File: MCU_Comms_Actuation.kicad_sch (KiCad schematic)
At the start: 46 parts, among them J1 MTSW-105-09-L-S-480, J2 U.FL-R-SMT-1_80_, Y2 C3E-8.000-18-3030-X-R

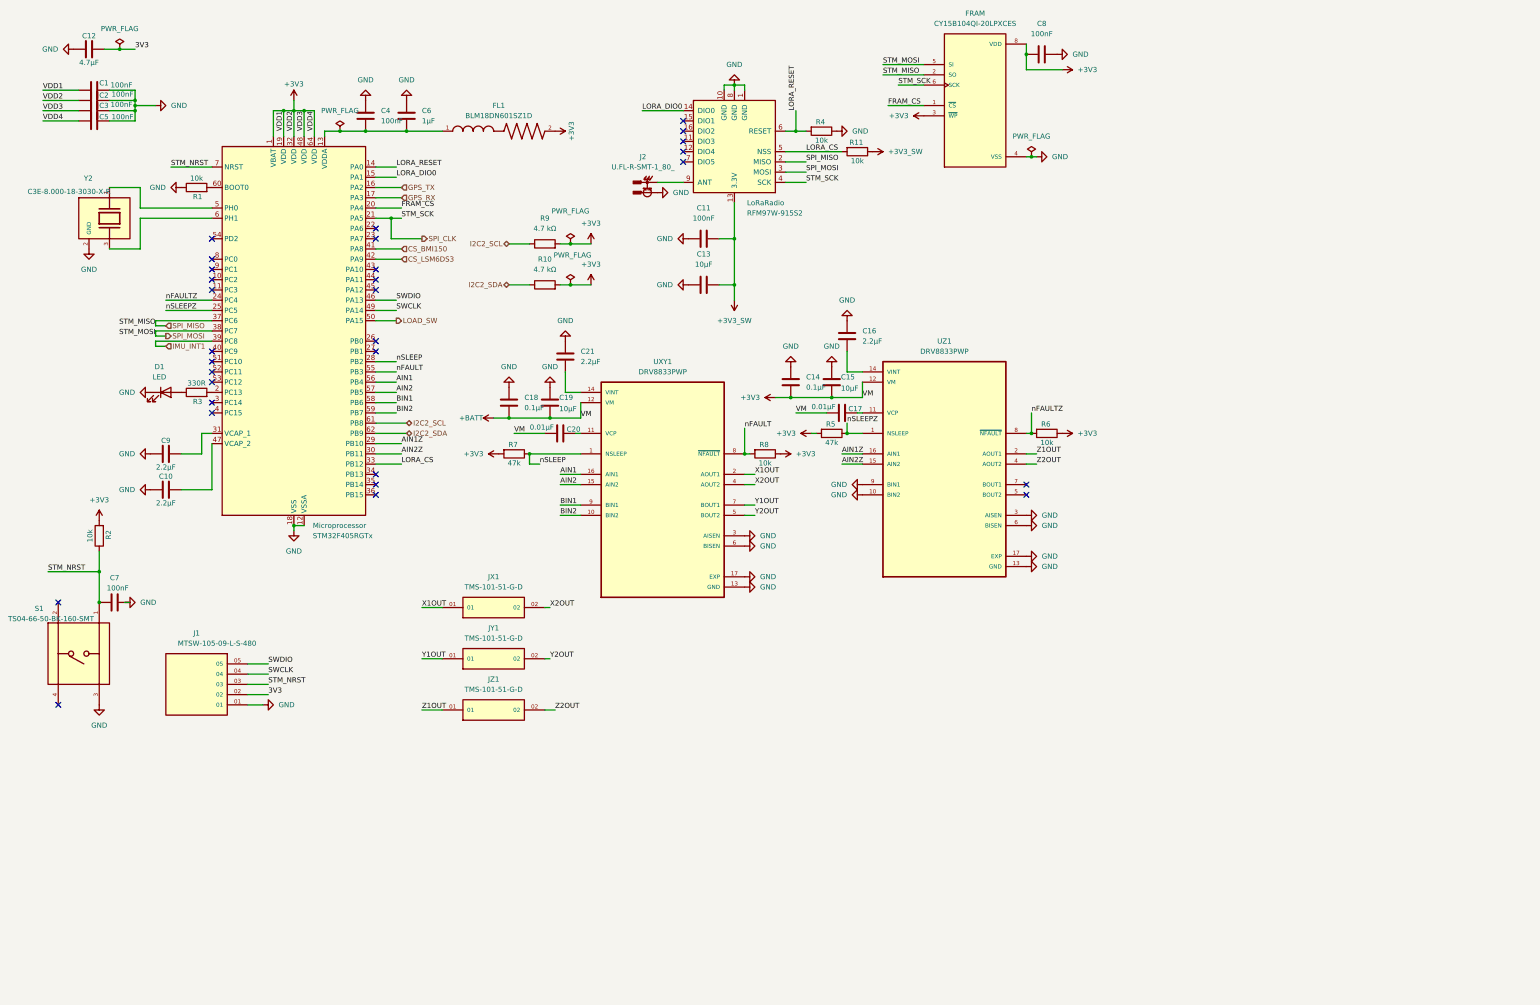
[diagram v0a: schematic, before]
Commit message: Add XYZ photodiodes to sun sensor. Fix hierarchical labels on MCU.
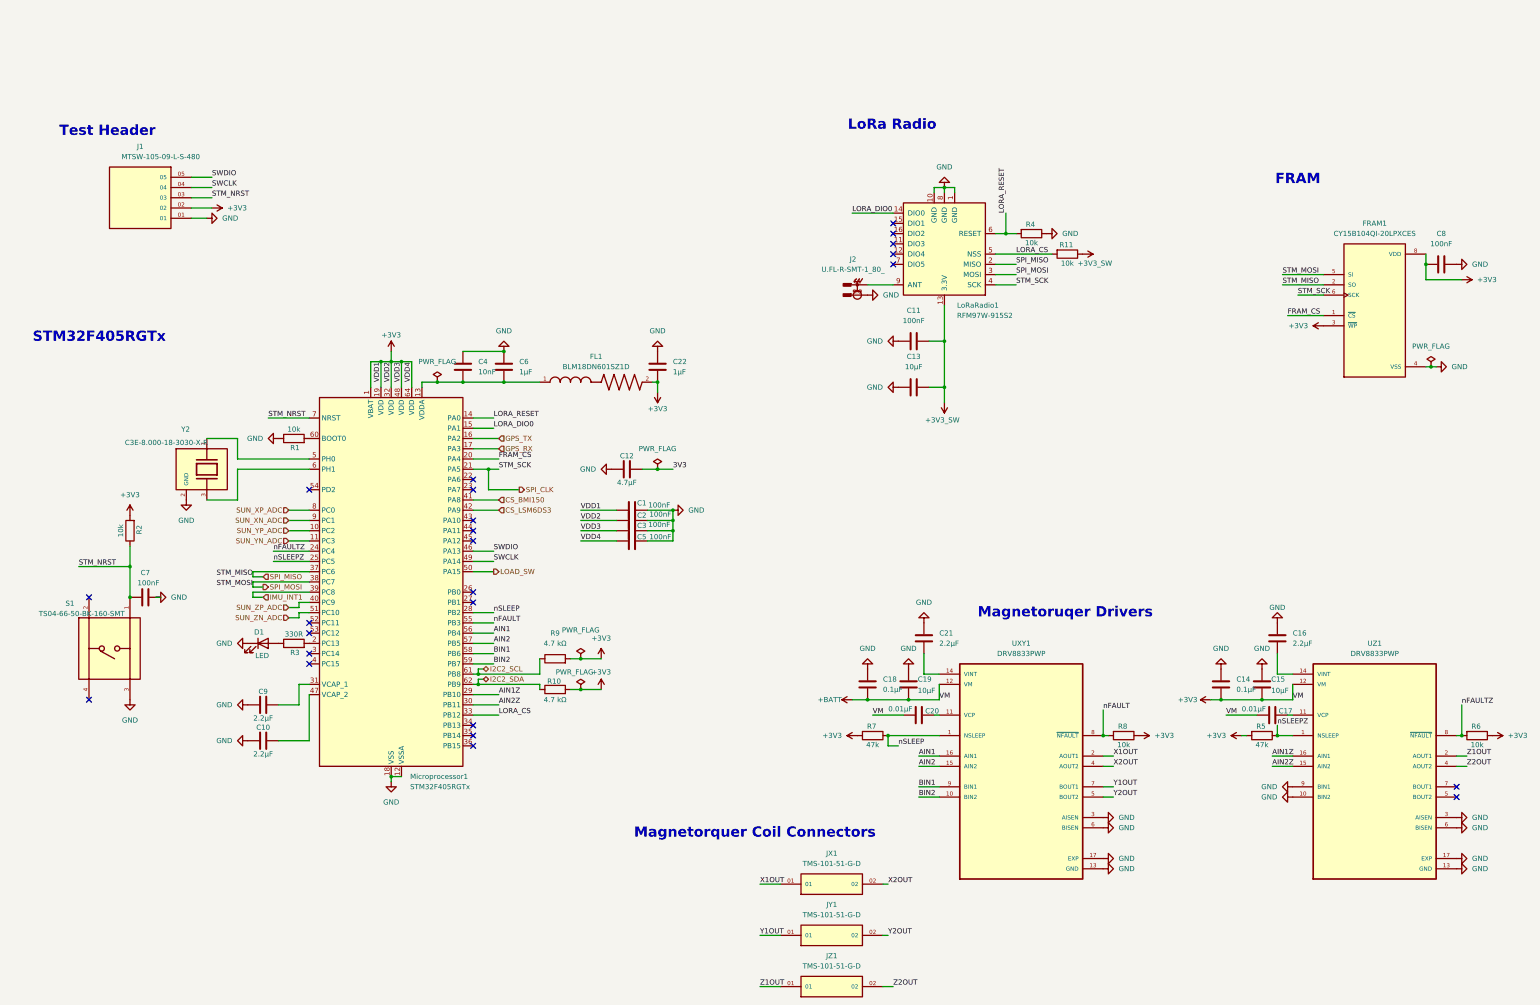
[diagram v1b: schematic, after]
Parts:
- added C22: 1µF, Capacitor_SMD:C_0603_1608Metric, symbol Device:C
- C4: value 100nF -> 10nF
- renumbered FRAM to FRAM1, LoRaRadio to LoRaRadio1, Microprocessor to Microprocessor1
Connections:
- net +3V3: now also J1.02, C22.2
- net 3V3: no longer J1.02
- net GND: now also C22.1
- net SUN_YP_ADC: now reaches Microprocessor1.10 (PC2)
- net SUN_YN_ADC: now reaches Microprocessor1.11 (PC3)
- net SUN_ZP_ADC: now reaches Microprocessor1.40 (PC9)
- net SUN_ZN_ADC: now reaches Microprocessor1.51 (PC10)
- net SUN_XP_ADC: now reaches Microprocessor1.8 (PC0)
- net SUN_XN_ADC: now reaches Microprocessor1.9 (PC1)
- no-connect marks 30 -> 24
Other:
- note added: "FRAM"
- note added: "LoRa Radio"
- note added: "Magnetorquer Coil Connectors"
- note added: "Magnetoruqer Drivers"
- note added: "STM32F405RGTx"
- note added: "Test Header"
- moved on the sheet: C1, C10, C11, C12, C13, C14, C15, C16, C17, C18, C19, C2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

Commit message: Fix sun sensor axis label mismatch
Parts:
- renumbered FRAM1 to FRAM, LoRaRadio1 to LoRaRadio, Microprocessor1 to Microprocessor
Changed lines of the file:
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@@
 	(wire
 		(pts
-			(xy 82.55 140.97) (xy 87.63 140.97)
+			(xy 78.74 140.97) (xy 87.63 140.97)
 		)
 		(stroke
@@
 	(wire
 		(pts
-			(xy 82.55 138.43) (xy 87.63 138.43)
+			(xy 78.74 138.43) (xy 87.63 138.43)
 		)
 		(stroke
@@
 	(wire
 		(pts
-			(xy 82.55 162.56) (xy 85.09 162.56)
+			(xy 78.74 162.56) (xy 85.09 162.56)
 		)
 		(stroke
@@
 	(wire
 		(pts
-			(xy 82.55 143.51) (xy 87.63 143.51)
+			(xy 78.74 143.51) (xy 87.63 143.51)
 		)
 		(stroke
@@
 	(wire
 		(pts
-			(xy 82.55 165.1) (xy 85.09 165.1)
+			(xy 78.74 165.1) (xy 85.09 165.1)
 		)
 		(stroke
@@
 	(wire
 		(pts
-			(xy 82.55 146.05) (xy 87.63 146.05)
+			(xy 78.74 146.05) (xy 87.63 146.05)
 		)
 		(stroke
@@
 	(hierarchical_label "SUN_XP_ADC"
 		(shape input)
-		(at 82.55 138.43 180)
+		(at 78.74 138.43 180)
 		(effects
 			(font
@@
 	(hierarchical_label "SUN_YP_ADC"
 		(shape input)
-		(at 82.55 143.51 180)
+		(at 78.74 143.51 180)
 		(effects
 			(font
@@
 	(hierarchical_label "SUN_XN_ADC"
 		(shape input)
-		(at 82.55 140.97 180)
+		(at 78.74 140.97 180)
 		(effects
 			(font
@@
 	(hierarchical_label "SUN_YN_ADC"
 		(shape input)
-		(at 82.55 146.05 180)
+		(at 78.74 146.05 180)
 		(effects
 			(font
@@
 	(hierarchical_label "SUN_ZN_ADC"
 		(shape input)
-		(at 82.55 165.1 180)
+		(at 78.74 165.1 180)
 		(effects
 			(font
@@
 	(hierarchical_label "SUN_ZP_ADC"
 		(shape input)
-		(at 82.55 162.56 180)
+		(at 78.74 162.56 180)
 		(effects
 			(font
@@
 				)
 			)
+			(project "DukeSatChip"
+				(path "/c9dca0a0-0655-45b8-af3d-da736a85b271/0dc59f70-6e74-4892-a502-b747b26099d8"
+					(reference "#PWR052")
+					(unit 1)
+				)
+			)
 		)
 	)
@@
 		(dnp no)
 		(fields_autoplaced yes)
-		(property "Reference" "FRAM1"
+		(property "Reference" "FRAM"
 			(at 351.79 67.31 0)
 			(show_name no)
@@
 		(dnp no)
 		(fields_autoplaced yes)
-		(property "Reference" "Microprocessor1"
+		(property "Reference" "Microprocessor"
 			(at 112.6333 204.47 0)
 			(show_name no)
@@
 				)
 			)
+			(project "DukeSatChip"
+				(path "/c9dca0a0-0655-45b8-af3d-da736a85b271/0dc59f70-6e74-4892-a502-b747b26099d8"
+					(reference "#PWR025")
+					(unit 1)
+				)
+			)
 		)
 	)
@@
 				)
 			)
+			(project "DukeSatChip"
+				(path "/c9dca0a0-0655-45b8-af3d-da736a85b271/0dc59f70-6e74-4892-a502-b747b26099d8"
+					(reference "#PWR010")
+					(unit 1)
+				)
+			)
 		)
 	)
@@
 		(dnp no)
 		(fields_autoplaced yes)
-		(property "Reference" "LoRaRadio1"
+		(property "Reference" "LoRaRadio"
 			(at 248.2281 87.63 0)
 			(show_name no)
@@
 				)
 			)
+			(project "DukeSatChip"
+				(path "/c9dca0a0-0655-45b8-af3d-da736a85b271/0dc59f70-6e74-4892-a502-b747b26099d8"
+					(reference "C22")
+					(unit 1)
+				)
+			)
 		)
 	)
@@
 		)
 	)
-	(embedded_fonts no)
 )
